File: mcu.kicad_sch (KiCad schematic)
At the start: 64 parts, among them P20 HEADER-2x11, P22 HEADER-2x13, P26 LPC_JTAG, P28 HEADER-2x11, SW1 SWITCH, SW2 SWITCH, U20 W25Q16, U23 LPC4330FET180, X2 MCU_XTAL, X3 RTC_XTAL

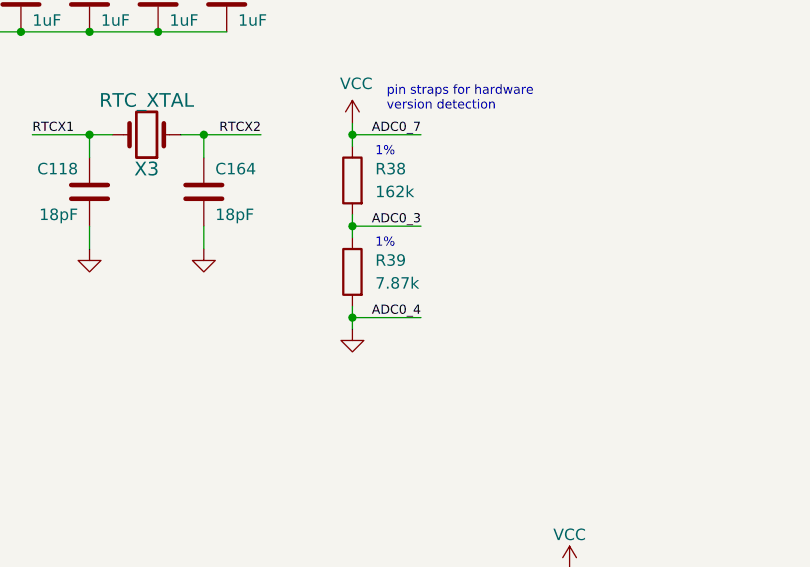
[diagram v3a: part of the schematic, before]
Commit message: Update hardware version detection pin strap
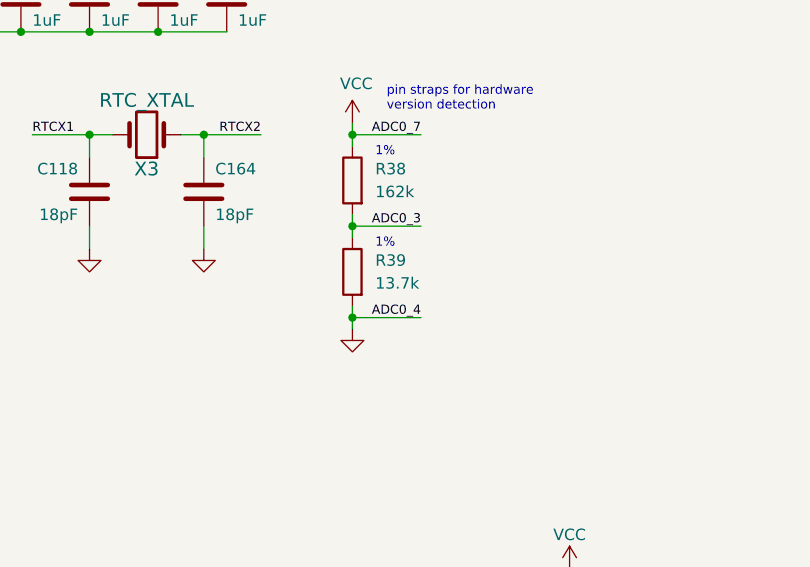
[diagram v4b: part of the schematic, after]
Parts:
- R39: value 7.87k -> 13.7k; Part Number RC0402FR-077K87L -> RC0402FR-0713K7L
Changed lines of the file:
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@@
 			)
 		)
-		(property "Value" "7.87k"
+		(property "Value" "13.7k"
 			(at 114.3 55.8799 0)
 			(effects
@@
 			)
 		)
-		(property "Description" "RES 7.87K OHM 1% 1/16W 0402"
+		(property "Description" "RES 13.7K OHM 1% 1/16W 0402"
 			(at 111.76 54.61 0)
 			(effects
@@
 			)
 		)
-		(property "Part Number" "RC0402FR-077K87L"
+		(property "Part Number" "RC0402FR-0713K7L"
 			(at 111.76 54.61 0)
 			(effects

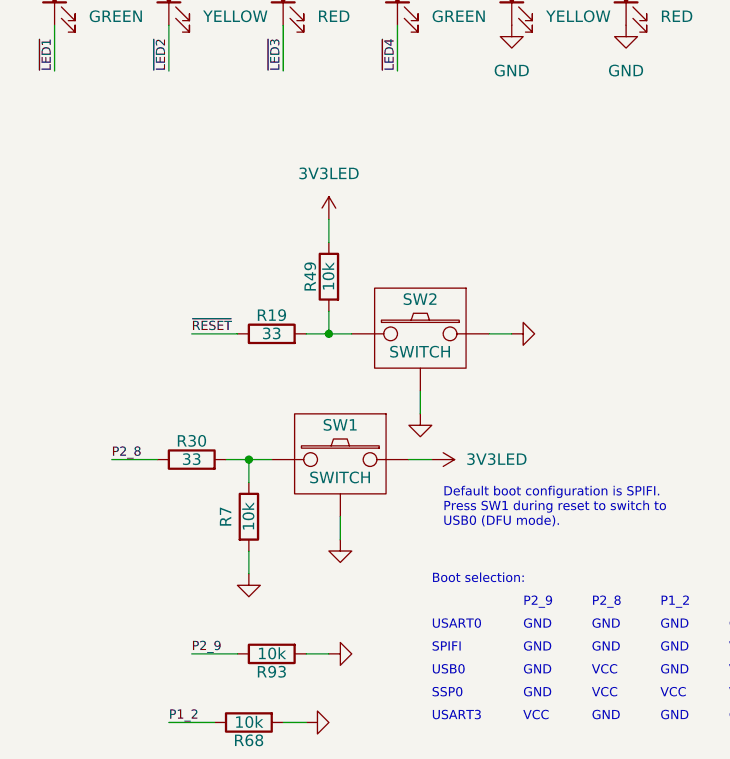
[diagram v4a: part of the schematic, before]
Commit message: Update tactile switch SW1, SW2 footprint
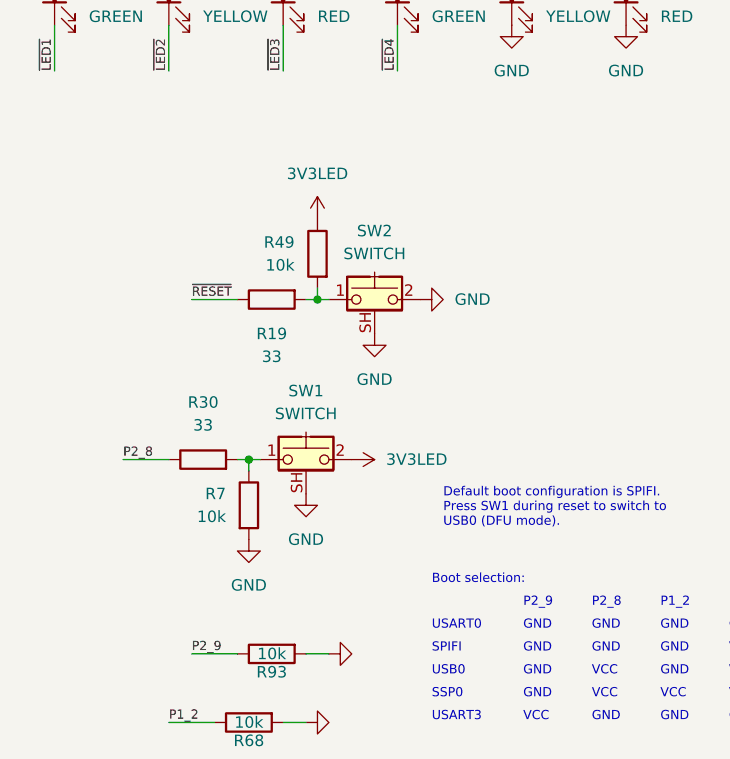
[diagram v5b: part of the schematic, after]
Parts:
- SW1, SW2: footprint hackrf:GSG-SWITCH-FSMRA -> praline:SW_Tactile_SPST_Angled_PTS645Vx58-2LFS; symbol hackrf:SW_PUSH_SHIELDED -> Switch:SW_Push_Shielded
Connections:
- net 3V3LED: now also SW1.2; no longer SW1.1
- net GND: now also SW1.SH (B), SW2.2, SW2.SH (B); no longer SW1.0 (SHIELD), SW2.0 (SHIELD), SW2.1
- net at R19.2, R49.2: now also SW2.1; no longer SW2.2
- net at R30.2, R7.1: now also SW1.1; no longer SW1.2
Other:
- moved on the sheet: R19, R30, R49, R7

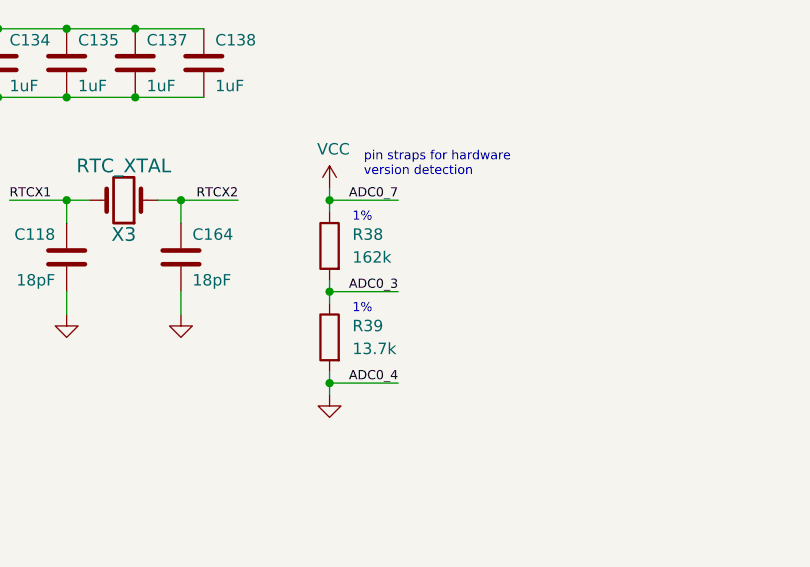
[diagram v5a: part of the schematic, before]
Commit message: Reduce antenna bias current limit to 125 mA
Change all 162k resistors to 180k
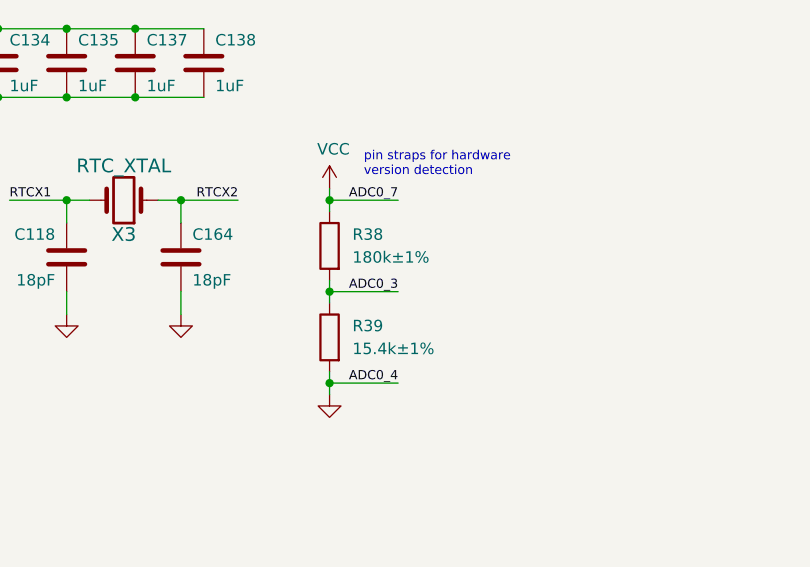
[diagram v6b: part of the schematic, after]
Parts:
- R38: value 162k -> 180k±1%; Part Number RC0402FR-07162KL -> RC0402FR-07180KL
- R39: value 13.7k -> 15.4k±1%; Part Number RC0402FR-0713K7L -> RC0402FR-0715K4L
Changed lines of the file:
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@@
 		)
 	)
-	(text "1%"
-		(exclude_from_sim no)
-		(at 114.3 52.07 0)
-		(effects
-			(font
-				(size 1.016 1.016)
-			)
-			(justify left bottom)
-		)
-	)
 	(text "pin straps for hardware\nversion detection"
 		(exclude_from_sim no)
@@
 		)
 	)
-	(text "1%"
-		(exclude_from_sim no)
-		(at 114.3 41.91 0)
-		(effects
-			(font
-				(size 1.016 1.016)
-			)
-			(justify left bottom)
-		)
-	)
 	(text "VCC"
 		(exclude_from_sim no)
@@
 			)
 		)
-		(property "Value" "13.7k"
+		(property "Value" "15.4k±1%"
 			(at 114.3 55.8799 0)
 			(effects
@@
 			)
 		)
-		(property "Description" "RES 13.7K OHM 1% 1/16W 0402"
+		(property "Description" "RES 15.4K OHM 1% 1/16W 0402"
 			(at 111.76 54.61 0)
 			(effects
@@
 			)
 		)
-		(property "Part Number" "RC0402FR-0713K7L"
+		(property "Part Number" "RC0402FR-0715K4L"
 			(at 111.76 54.61 0)
 			(effects
@@
 			)
 		)
-		(property "Value" "162k"
+		(property "Value" "180k±1%"
 			(at 114.3 45.7199 0)
 			(effects
@@
 			)
 		)
-		(property "Description" "RES 1/16W 162K OHM 1% 0402"
+		(property "Description" "RES 180K OHM 1% 1/16W 0402"
 			(at 111.76 44.45 0)
 			(effects
@@
 			)
 		)
-		(property "Part Number" "RC0402FR-07162KL"
+		(property "Part Number" "RC0402FR-07180KL"
 			(at 111.76 44.45 0)
 			(effects

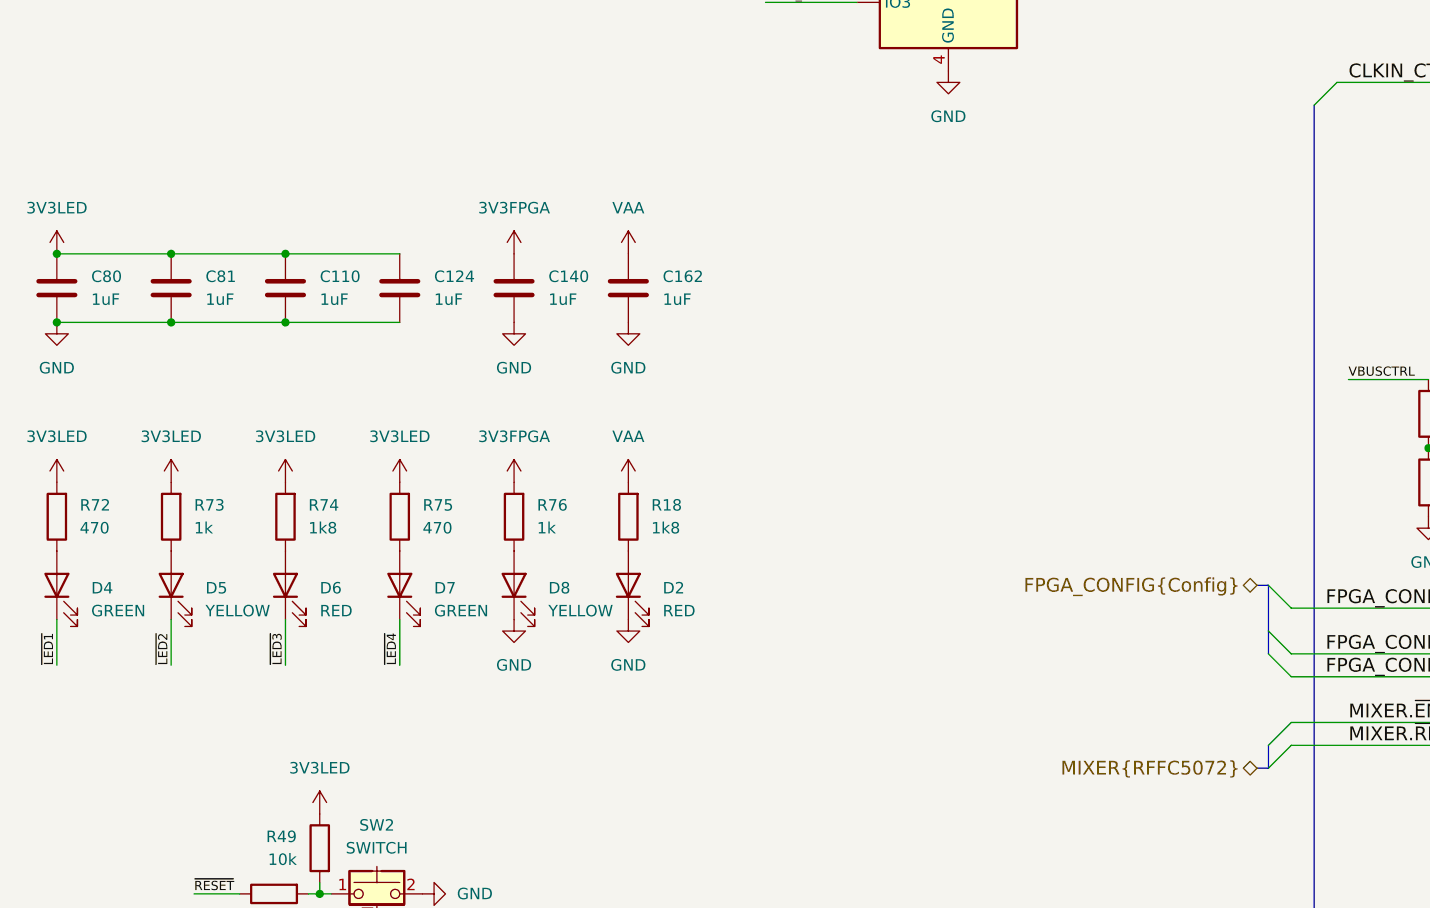
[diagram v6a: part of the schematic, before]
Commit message: Update LED component selections and colors
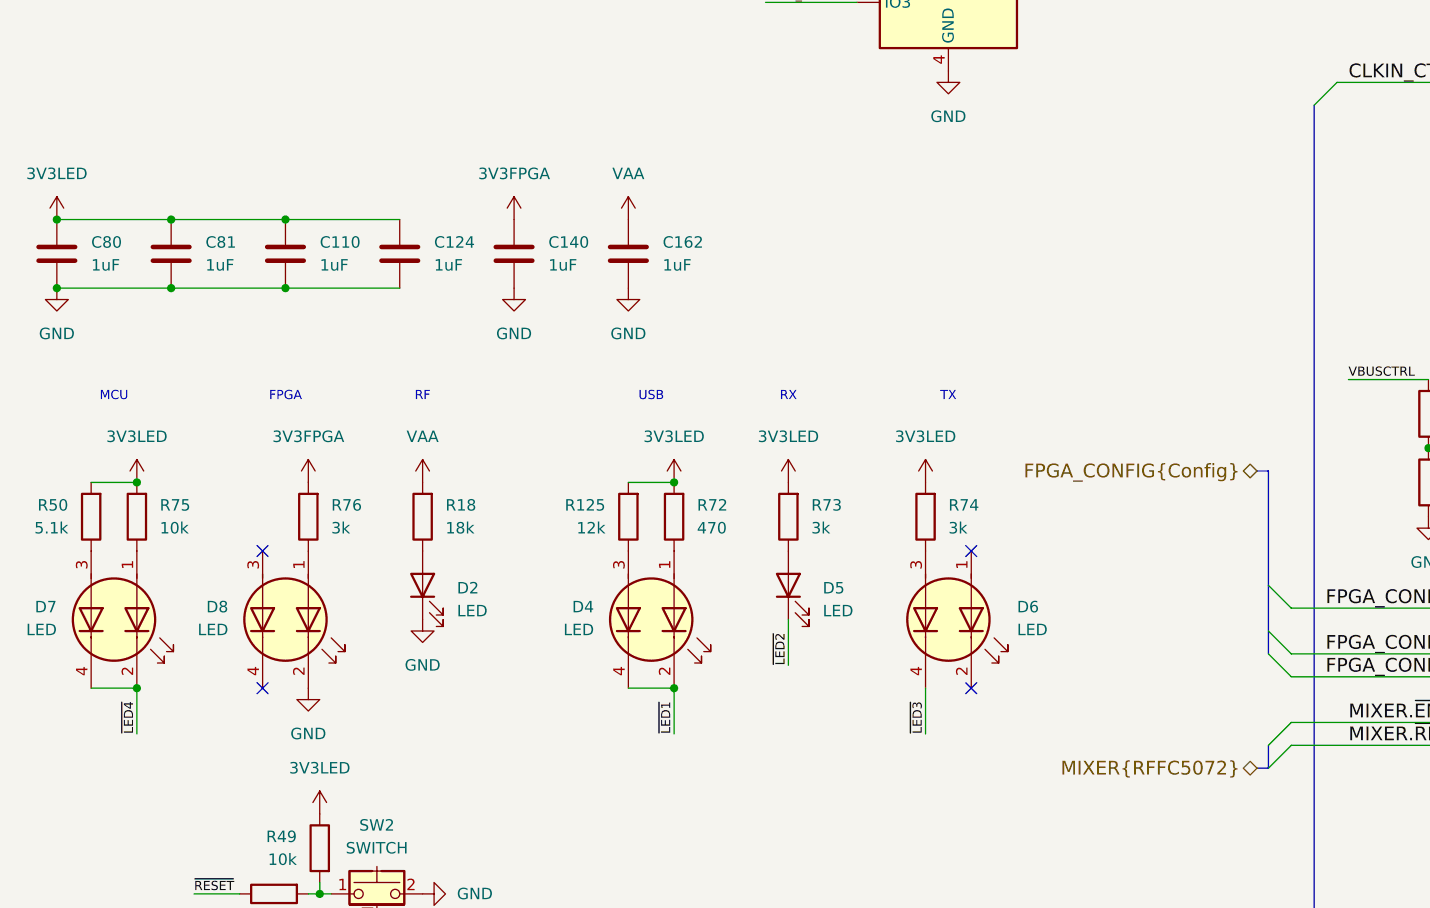
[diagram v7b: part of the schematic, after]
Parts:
- removed D4, D7: GREEN, gsg-modules:LTST-S220, symbol Device:LED
- removed D6: RED, gsg-modules:LTST-S220, symbol Device:LED
- removed D8: YELLOW, gsg-modules:LTST-S220, symbol Device:LED
- added D4, D6, D7, D8: LED, praline:LED_Dual_Xinglight_XL-3210_Horizontal, symbol Device:LED_Dual_AKAK
- added R125: 12k, Resistor_SMD:R_0402_1005Metric, symbol Device:R
- added R50: 5.1k, Resistor_SMD:R_0402_1005Metric, symbol Device:R
- D2: value RED -> LED; footprint gsg-modules:LTST-S220 -> praline:LED_Single_Xinglight_XL-3210_Horizontal; Manufacturer Lite-On -> Xinglight; Part Number LTST-S220KRKT -> XL-3210UGC
- D5: value YELLOW -> LED; footprint gsg-modules:LTST-S220 -> praline:LED_Single_Xinglight_XL-3210_Horizontal; Manufacturer Lite-On -> Xinglight; Part Number LTST-S220KSKT -> XL-3210UOC
- R18: value 1k8 -> 18k; Part Number RC0402JR-071K8L -> RC0402JR-0718KL
- R73, R76: value 1k -> 3k; footprint Resistor_SMD:R_0201_0603Metric -> Resistor_SMD:R_0402_1005Metric; Part Number RC0201FR-071KL -> RC0402JR-073KL
- R74: value 1k8 -> 3k; Part Number RC0402JR-071K8L -> RC0402JR-073KL
- R75: value 470 -> 10k; footprint Resistor_SMD:R_0201_0603Metric -> Resistor_SMD:R_0402_1005Metric; Part Number RC0201JR-07470RL -> RC0402JR-0710KL
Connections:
- net 3V3LED: now also R125.2, R50.2
- net GND: now also D8.2 (K1)
- net ~{LED1}: now also D4.2 (K1), D4.4 (K2)
- net ~{LED3}: now also D6.4 (K2)
- net ~{LED4}: now also D7.2 (K1), D7.4 (K2)
- net at R74.1: now also D6.3 (A2)
- net at R75.1: now also D7.1 (A1)
- net at R72.1: now also D4.1 (A1)
- net at R76.1: now also D8.1 (A1)
- new net: D7.3 (A2), R50.1
- new net: D4.3 (A2), R125.1
- no-connect marks 21 -> 25
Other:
- note added: "FPGA"
- note added: "MCU"
- note added: "RF"
- note added: "RX"
- note added: "TX"
- note added: "USB"
- moved on the sheet: C110, C124, C140, C162, C80, C81, D2, D5, R18, R72, R73, R74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

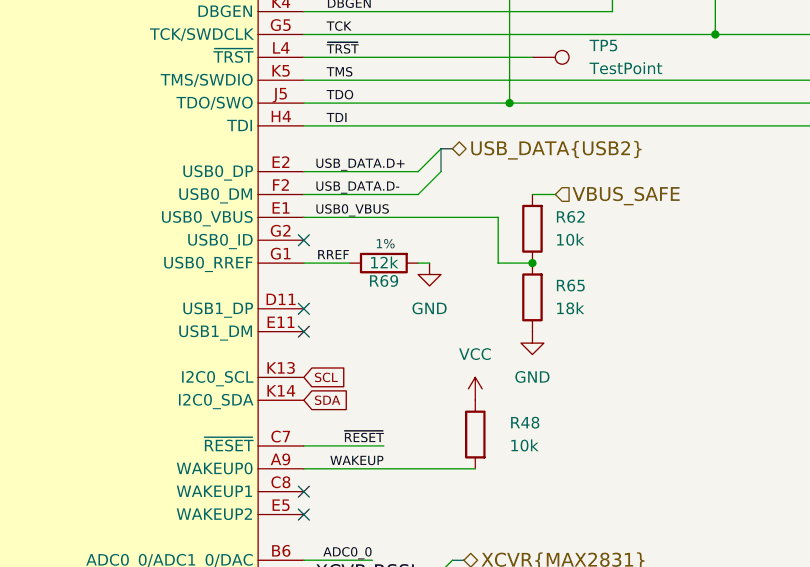
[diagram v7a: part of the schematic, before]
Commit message: Set TX baseband common-mode voltage with REFIN
- Do not populate TX baseband voltage divider
- Remove baseband DC block
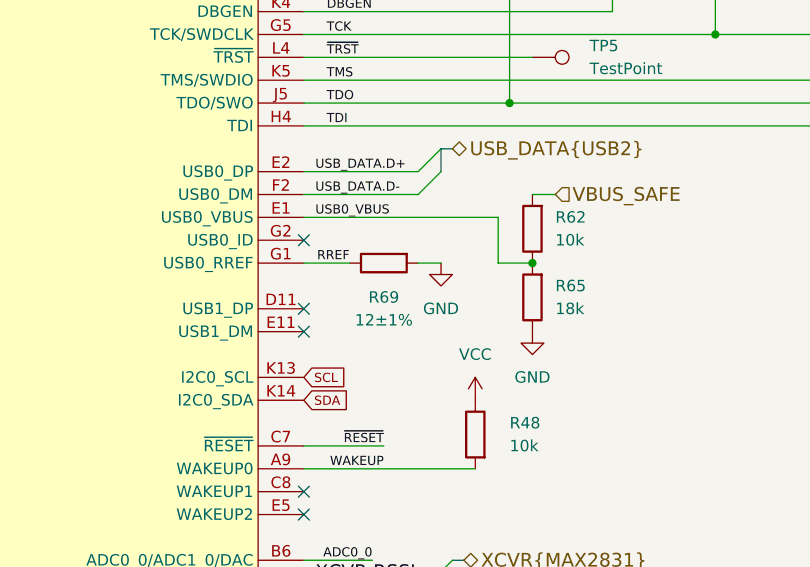
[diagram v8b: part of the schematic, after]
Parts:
- R125: footprint Resistor_SMD:R_0402_1005Metric -> Resistor_SMD:R_0201_0603Metric; Part Number RC0402FR-0712KL -> RC0201FR-0712KL
- R69: value 12k -> 12±1%; footprint Resistor_SMD:R_0402_1005Metric -> Resistor_SMD:R_0201_0603Metric; Part Number RC0402FR-0712KL -> RC0201FR-0712KL
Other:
- note removed: "1%"
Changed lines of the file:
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@@
 	(wire
 		(pts
-			(xy 257.81 177.8) (xy 259.08 177.8)
+			(xy 257.81 177.8) (xy 260.35 177.8)
 		)
 		(stroke
@@
 		)
 	)
-	(text "1%"
-		(exclude_from_sim no)
-		(at 255.27 176.53 0)
-		(effects
-			(font
-				(size 1.016 1.016)
-			)
-			(justify right bottom)
-		)
-	)
 	(text "USB0"
 		(exclude_from_sim no)
@@
 		(on_board yes)
 		(dnp no)
+		(fields_autoplaced yes)
 		(property "Reference" "R69"
-			(at 254 179.832 90)
+			(at 254 181.61 90)
 			(effects
 				(font
@@
 			)
 		)
-		(property "Value" "12k"
-			(at 254 177.8 90)
+		(property "Value" "12±1%"
+			(at 254 184.15 90)
 			(effects
 				(font
@@
 			)
 		)
-		(property "Footprint" "Resistor_SMD:R_0402_1005Metric"
+		(property "Footprint" "Resistor_SMD:R_0201_0603Metric"
 			(at 254 177.8 0)
 			(effects
@@
 			)
 		)
-		(property "Description" "RES 12K OHM 1% 1/16W 0402"
+		(property "Description" "RES 12K OHM 1% 1/20W 0201"
 			(at 254 177.8 0)
 			(effects
@@
 			)
 		)
-		(property "Part Number" "RC0402FR-0712KL"
+		(property "Part Number" "RC0201FR-0712KL"
 			(at 254 177.8 0)
 			(effects
@@
 			)
 		)
-		(property "Footprint" "Resistor_SMD:R_0402_1005Metric"
+		(property "Footprint" "Resistor_SMD:R_0201_0603Metric"
 			(at 83.82 167.64 0)
 			(effects
@@
 			)
 		)
-		(property "Description" "RES 12K OHM 1% 1/16W 0402"
+		(property "Description" "RES 12K OHM 1% 1/20W 0201"
 			(at 83.82 167.64 0)
 			(effects
@@
 			)
 		)
-		(property "Part Number" "RC0402FR-0712KL"
+		(property "Part Number" "RC0201FR-0712KL"
 			(at 83.82 167.64 0)
 			(effects
@@
 	(symbol
 		(lib_id "power:GND")
-		(at 259.08 177.8 0)
+		(at 260.35 177.8 0)
 		(unit 1)
 		(exclude_from_sim no)
@@
 		(fields_autoplaced yes)
 		(property "Reference" "#PWR0165"
-			(at 259.08 184.15 0)
+			(at 260.35 184.15 0)
 			(effects
 				(font
@@
 		)
 		(property "Value" "GND"
-			(at 259.08 182.88 0)
+			(at 260.35 182.88 0)
 			(effects
 				(font
@@
 		)
 		(property "Footprint" ""
-			(at 259.08 177.8 0)
+			(at 260.35 177.8 0)
 			(effects
 				(font
@@
 		)
 		(property "Datasheet" ""
-			(at 259.08 177.8 0)
+			(at 260.35 177.8 0)
 			(effects
 				(font
@@
 		)
 		(property "Description" "Power symbol creates a global label with name \"GND\" , ground"
-			(at 259.08 177.8 0)
+			(at 260.35 177.8 0)
 			(effects
 				(font
